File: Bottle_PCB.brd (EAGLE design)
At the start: 100 x 50 mm, 96 parts, among them IC1 LP2985-33DBV, J1 GROVE-4P-2.0-SMD, Q1 8.000 MHz, Q5 ZVN 3306 F, Q6 ZVN 3306 F, Q7 ZVN 3306 F, U1 USD-SOCKETNEW, U3 CN3065-1320040P1

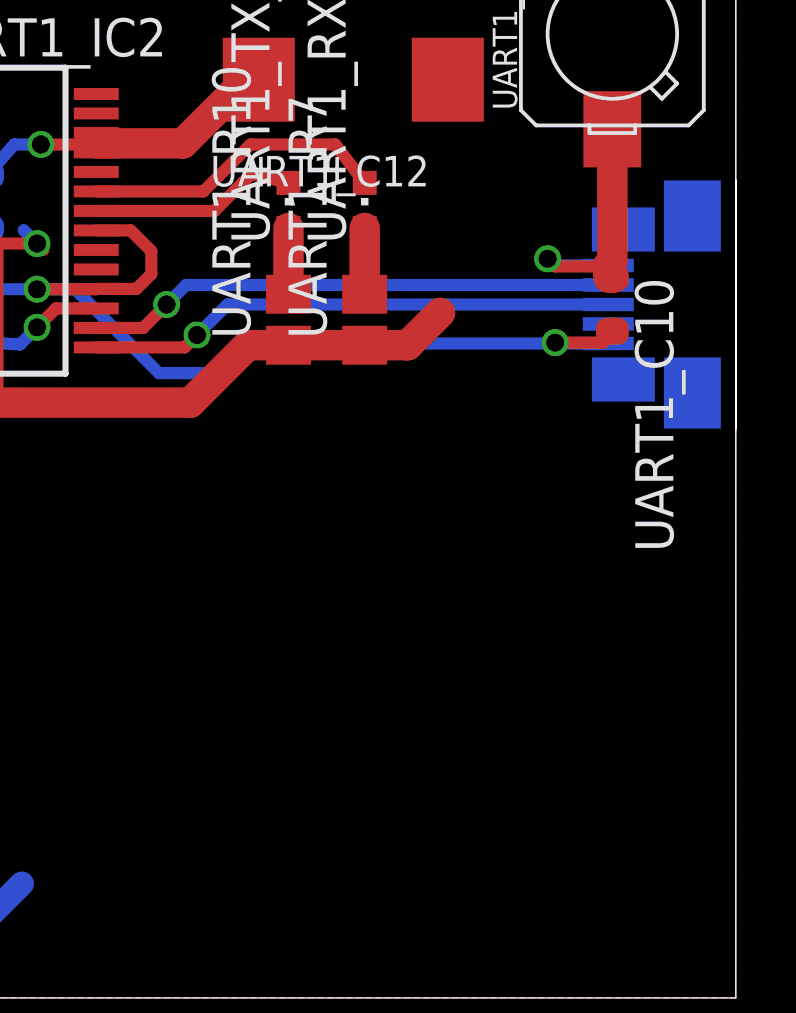
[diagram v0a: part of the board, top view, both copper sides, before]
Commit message: - replaces mini USB B connector with SparkFun version
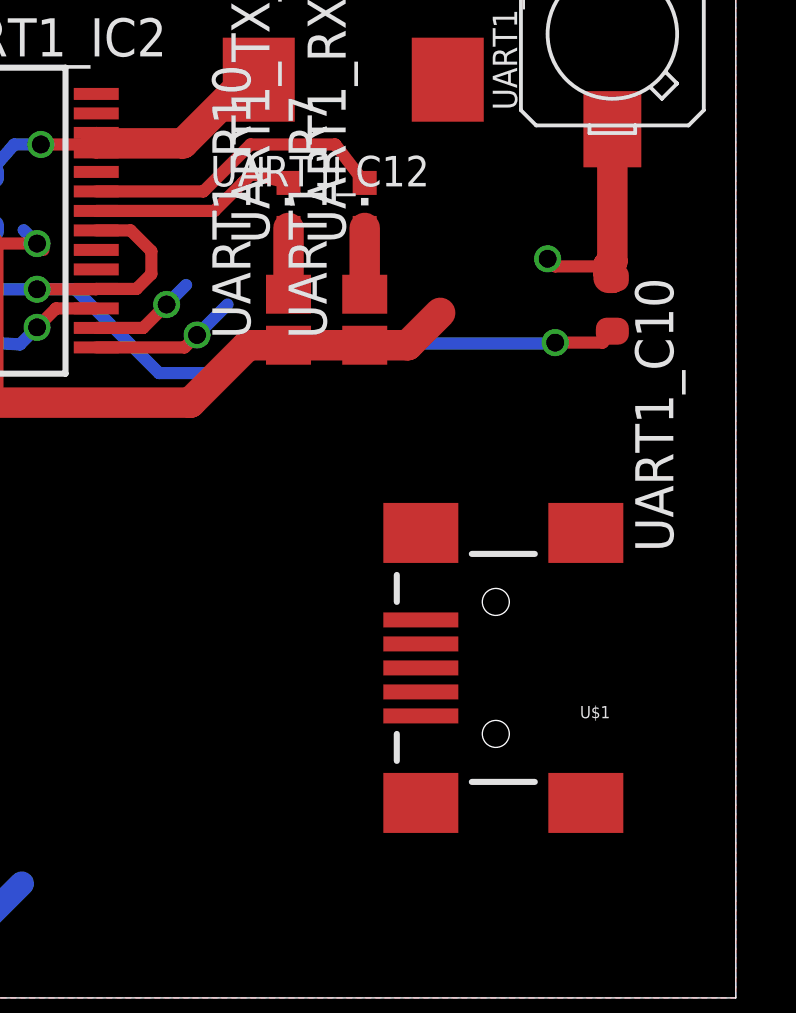
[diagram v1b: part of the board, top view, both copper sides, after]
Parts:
- removed USB1: MOLEX-47346-0001, usb_con-update:MOLEX-47364-0001
- added U$1: USB-MINIB-5PIN, SparkFun-Connectors:USB-MINIB
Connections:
- net GND: now also U$1.GND; no longer USB1.5
- net N$10: now also U$1.D+; no longer USB1.3
- net N$12: now also U$1.VBUS; no longer USB1.1
- net N$4: now also U$1.D-; no longer USB1.2
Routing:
- net N$4: track 17.7 -> 3.59 mm
- net N$10: track 17.7 -> 4.97 mm
- net N$12: track 9.74 -> 7.93 mm
- net GND: track 331.2 -> 329.5 mm
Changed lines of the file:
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@@
 <attribute name="OC_FARNELL" value="176432" x="58.1025" y="3.4925" size="1.778" layer="27" rot="R180" display="off"/>
-</element>
-<element name="USB1" library="usb_con-update" package="MOLEX-47364-0001" value="MOLEX-47346-0001" x="98.552" y="23.114" smashed="yes" rot="MR0">
-<attribute name="NAME" x="99.802" y="27.714" size="1.27" layer="22" rot="MR0"/>
 </element>
 <element name="D1" library="diode" package="SOD-123_MINI-SMA" value="CGRM4001-G" x="57.4675" y="10.4775" rot="R90"/>
@@
 <element name="C_V_LIPO_USB" library="_E" package="SMC_D" value="10µ/10V" x="-65" y="-301"/>
 <element name="UART1_C1" library="Arduino-SmartPrj" package="C0603-ROUND" value="10n" x="-68" y="-308"/>
+<element name="U$1" library="SparkFun-Connectors" package="USB-MINIB" value="USB-MINIB-5PIN" x="92" y="11" rot="R180"/>
 </elements>
 <signals>
@@
 <contactref element="RESET_SW" pad="2"/>
 <wire x1="78.682" y1="28.183" x2="78.682" y2="28.48479375" width="0.4064" layer="1"/>
-<contactref element="USB1" pad="5"/>
 <contactref element="C2" pad="1"/>
 <contactref element="C3" pad="1"/>
@@
 <wire x1="76.708" y1="23.622" x2="75.118" y2="23.622" width="0.4064" layer="16"/>
 <wire x1="75.118" y1="23.622" x2="75.057" y2="23.622" width="0.4064" layer="16"/>
-<wire x1="95.752" y1="21.814" x2="94.01" y2="21.814" width="0.4064" layer="16"/>
 <wire x1="94.01" y1="21.814" x2="93.98" y2="21.844" width="0.4064" layer="16"/>
 <via x="93.98" y="21.844" extent="1-16" drill="0.6"/>
@@
 <contactref element="C_V_LIPO_USB" pad="-"/>
 <contactref element="UART1_C1" pad="2"/>
+<contactref element="U$1" pad="GND"/>
 <wire x1="-44" y1="-175.25" x2="-47.95" y2="-183" width="0" layer="19" extent="1-1"/>
 <wire x1="-44" y1="-168.25" x2="-44" y2="-175.25" width="0" layer="19" extent="1-1"/>
@@
 <wire x1="55" y1="35" x2="51.1175" y2="41.5925" width="0" layer="19" extent="1-1"/>
 <wire x1="3" y1="16" x2="1.4405" y2="25.568" width="0" layer="19" extent="1-1"/>
+<wire x1="89.5" y1="12.6" x2="94.01" y2="21.814" width="0" layer="19" extent="1-16"/>
 </signal>
 <signal name="AREF">
@@
 <signal name="N$4">
 <contactref element="UART1_IC2" pad="16"/>
-<contactref element="USB1" pad="2"/>
-<wire x1="95.752" y1="23.764" x2="81.676" y2="23.764" width="0.4064" layer="16"/>
 <wire x1="81.676" y1="23.764" x2="81.026" y2="23.114" width="0.4064" layer="16"/>
 <via x="81.026" y="23.114" extent="1-16" drill="0.6"/>
 <wire x1="81.026" y1="23.114" x2="80.245" y2="22.333" width="0.4064" layer="1"/>
 <wire x1="80.245" y1="22.333" x2="78.682" y2="22.333" width="0.4064" layer="1"/>
+<contactref element="U$1" pad="D-"/>
+<wire x1="80.245" y1="22.333" x2="89.5" y2="10.2" width="0" layer="19" extent="1-1"/>
 </signal>
 <signal name="N$10">
 <contactref element="UART1_IC2" pad="15"/>
-<contactref element="USB1" pad="3"/>
-<wire x1="95.752" y1="23.114" x2="83.058" y2="23.114" width="0.4064" layer="16"/>
 <wire x1="83.058" y1="23.114" x2="82.042" y2="22.098" width="0.4064" layer="16"/>
 <via x="82.042" y="22.098" extent="1-16" drill="0.6"/>
 <wire x1="82.042" y1="22.098" x2="81.627" y2="21.683" width="0.4064" layer="1"/>
 <wire x1="81.627" y1="21.683" x2="78.682" y2="21.683" width="0.4064" layer="1"/>
+<contactref element="U$1" pad="D+"/>
+<wire x1="81.627" y1="21.683" x2="89.5" y2="11" width="0" layer="19" extent="1-1"/>
 </signal>
 <signal name="N$11">
@@
 <contactref element="UART1_C10" pad="1"/>
 <contactref element="UART1_L2" pad="1"/>
-<contactref element="USB1" pad="1"/>
 <wire x1="95.758" y1="24.003" x2="95.885" y2="24.003" width="1.016" layer="1"/>
 <wire x1="95.885" y1="28.956" x2="95.885" y2="24.547" width="1.016" layer="1"/>
@@
 <wire x1="95.752" y1="24.414" x2="95.752" y2="24.197" width="1.016" layer="1"/>
 <wire x1="95.752" y1="24.197" x2="95.885" y2="24.003" width="1.016" layer="1"/>
-<wire x1="95.752" y1="24.414" x2="93.95" y2="24.414" width="0.4064" layer="16"/>
 <wire x1="93.95" y1="24.414" x2="93.726" y2="24.638" width="0.4064" layer="16"/>
 <via x="93.726" y="24.638" extent="1-16" drill="0.6"/>
@@
 <wire x1="93.98" y1="24.384" x2="95.565" y2="24.384" width="0.4064" layer="1"/>
 <wire x1="95.565" y1="24.384" x2="95.885" y2="24.003" width="0.4064" layer="1"/>
+<contactref element="U$1" pad="VBUS"/>
+<wire x1="89.5" y1="9.4" x2="93.98" y2="24.384" width="0" layer="19" extent="1-1"/>
 </signal>
 <signal name="N$13">

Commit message: - cleaned up and unified many discrete components - set Reichelt Order Numbers for all capacitors
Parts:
- removed D1: CGRM4001-G, diode:SOD-123_MINI-SMA
- removed UART1_D_RESET: 1N4848, _D:MINIMELF
- added D5, D6: MSS1P2U, Seed-Discrete:D1005
- added R_WAKEUP: 10k, Arduino-SmartPrj:R0603-ROUND
- C1, C11, C12, C16, C2, C3, C4, C6, C7, C8, C9: device quantum-sensor:C0805 -> Arduino-SmartPrj:C0603-ROUND
- C10, C5: device rcl:SMC_D -> Arduino-SmartPrj:C1210
- C13: device rcl:C0805 -> Arduino-SmartPrj:C1210
- C14, C15: device resistor:C0603 -> Arduino-SmartPrj:C0603-ROUND
- R1, R10, R11, R16, R17, R18, R19, R20, R21: device rcl:R0603 -> Arduino-SmartPrj:R0603-ROUND
- R12, R13: value 4k7 -> 10k; device resistor:R0603 -> Arduino-SmartPrj:R0603-ROUND
- R14, R15, R8, R9: device resistor:R0603 -> Arduino-SmartPrj:R0603-ROUND
- R2, R3, R4, R5, R6, R7: device rcl:M1206 -> Arduino-SmartPrj:R0603-ROUND
- R_RESET, UART1_R10, UART1_R7: device quantum-sensor:R0805 -> Arduino-SmartPrj:R0603-ROUND
- UART1_R6: device _R:R0805 -> Arduino-SmartPrj:R0603-ROUND
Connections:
- new net N$16: C12.2, R_WAKEUP.1, SW_WAKEUP.3, SW_WAKEUP.4
- net +3V3: now also D6.-; no longer D1.C
- net BEE_VCC: now also C10.1; no longer C10.+
- net FTDI_DTR: now also D5.-; no longer UART1_D_RESET.C
- net GND: now also C10.2, C5.2; no longer C10.-, C5.-
- net MCU_RST: now also D5.+, D6.+; no longer D1.A, UART1_D_RESET.A
- net N$31: now also C5.1; no longer C5.+
- net PB1_INT_BUTTON: no longer C12.2, SW_WAKEUP.3, SW_WAKEUP.4
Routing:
- net GND: track 329.5 -> 294.3 mm, vias 26 -> 25
- net MCU_RST: track 72.3 -> 60.3 mm
- net +3V3: track 266.4 -> 255.2 mm, vias 10 -> 9
- net PB1_INT_BUTTON: track 10.2 -> 0.00 mm
- net N$31: track 24.6 -> 26.4 mm
- net N$33: track 33.5 -> 35.2 mm
- net PC2_SD_OFF: track 22.3 -> 22.8 mm

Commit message: - unified, replaced and checked all components - added vendor IDs and order information to all components - generated BOMs
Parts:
- removed C_3V3, C_VIN, C_V_LIPO_USB: 10µ/10V, _E:SMC_D
- removed UART1_C12: 10µ, _E:SMC_D
- added C17, C18, C19, C20: 10µF / 16V, Arduino-SmartPrj:C0805
- ATMEGA1284P-AU: value ATMEGA644A -> Reichelt ATMEGA 1284P-AU
- GROOVE_A6_A7, GROOVE_D7_D8, GROOVE_I2C: value GROVE-4P-2.0-SMD -> GROVE-4P-2.0-SMD Seed ACC39145O
- IC1: value LP2985-33DBV -> LP2985-33DBV, Farnell 2395925
- ISP1: value AVRISP-6 -> Reichelt WSL 6G
- Q1: value 8.000 MHz -> 16.000 MHz; device crystal:HC18U-V -> crystal:HC49U-V
- Q5, Q6, Q7: value ZVN 3306 F -> Reichelt ZVN 3306 F
- R17: value 330 (20mA) or 2k -> 330 (20mA) or 2k2
- R5: value 20k -> 10k
- T_LIPO_USB: value (none) -> Reichelt IRLML 6402
- U1: value USD-SOCKETNEW -> Sparkfun PRT-00127
- U2: value (none) -> Seed BLE Bee - Based on HM-11 Module sowie Bluetooth V4.0 HM-11 BLE Module
- U3: value CN3065-1320040P1 -> CN3065-1320040P1, Aliexpress Such as rhyme new original CN3065 DFN8 lithium battery charge management / protection chip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
- UART1_IC2: value FT232RL -> Reichelt FT 232 RL
- UART1_L2: device _Trafo_Spule:PIS2408 -> rcl:L1812
- UART1_R10, UART1_R7: value 1k -> 2k2
- USB_CONNECTOR: value USB-MINIB-5PIN -> USB-MINIB-5PIN Sparkfun PRT-00587
- XBEE_SOCKET: value XBEE-1B3 -> 2x Reichelt BL 1X10G SMD2,00
- renumbered ATMEGA1284 to ATMEGA1284P-AU, J1 to GROOVE_A6_A7, U$1 to USB_CONNECTOR
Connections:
- net +3V3: now also C18.1; no longer C_3V3.+
- net +5V: now also C20.1; no longer UART1_C12.+
- net GND: now also C17.2, C18.2, C19.2, C20.2; no longer C_3V3.-, C_VIN.-, C_V_LIPO_USB.-, UART1_C12.-
- net VIN: now also C19.1; no longer C_VIN.+
- net V_LIPO_USB: now also C17.1; no longer C_V_LIPO_USB.+
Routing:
- net N$12: track 7.93 -> 9.16 mm

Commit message: - merged BOMs - BOM_Merged.csv is checked for correctness and completeness - minor adjustments in Device Values for unification
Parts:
- C1: value 22p -> 22pF
- C10, C5: value 1µ -> 1µF
- C11, C12, C2, C3, C4, C6, C7, C8, UART1_C11, UART1_C2: value 100n -> 100nF
- C9: value 22p -> 22pf
- UART1_C10: value 10n -> 10nF
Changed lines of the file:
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@@
 <attribute name="VALUE" x="55.88" y="11.7475" size="1.27" layer="27" rot="R90"/>
 </element>
-<element name="C9" library="Arduino-SmartPrj" package="C0603-ROUND" value="22p" x="61.2648" y="20.8788" smashed="yes" rot="R270">
+<element name="C9" library="Arduino-SmartPrj" package="C0603-ROUND" value="22pf" x="61.2648" y="20.8788" smashed="yes" rot="R270">
 <attribute name="NAME" x="62.5348" y="22.1488" size="1.27" layer="25" rot="R270"/>
 <attribute name="VALUE" x="60.6298" y="19.6088" size="1.27" layer="27" rot="R270"/>
 </element>
-<element name="C1" library="Arduino-SmartPrj" package="C0603-ROUND" value="22p" x="61.2648" y="24.3078" smashed="yes" rot="R90">
+<element name="C1" library="Arduino-SmartPrj" package="C0603-ROUND" value="22pF" x="61.2648" y="24.3078" smashed="yes" rot="R90">
 <attribute name="NAME" x="59.9948" y="23.0378" size="1.27" layer="25" rot="R90"/>
 <attribute name="VALUE" x="62.2173" y="25.5778" size="1.27" layer="27" rot="R90"/>
 </element>
-<element name="C7" library="Arduino-SmartPrj" package="C0603-ROUND" value="100n" x="36.5125" y="21.59" smashed="yes" rot="R270">
+<element name="C7" library="Arduino-SmartPrj" package="C0603-ROUND" value="100nF" x="36.5125" y="21.59" smashed="yes" rot="R270">
 <attribute name="NAME" x="37.7825" y="22.86" size="1.27" layer="25" rot="R270"/>
 <attribute name="VALUE" x="38.735" y="20.0025" size="1.27" layer="27" rot="R90"/>
@@
 <attribute name="OC_FARNELL" value="1455123" x="46.0375" y="21.2725" size="1.778" layer="27" rot="R180" display="off"/>
 </element>
-<element name="C6" library="Arduino-SmartPrj" package="C0603-ROUND" value="100n" x="47.625" y="21.59" rot="MR180"/>
+<element name="C6" library="Arduino-SmartPrj" package="C0603-ROUND" value="100nF" x="47.625" y="21.59" rot="MR180"/>
 <element name="UART1_IC2" library="FTDI" package="SSOP28" value="Reichelt FT 232 RL" x="75.057" y="25.908" rot="R270"/>
-<element name="UART1_C2" library="Arduino-SmartPrj" package="C0603-ROUND" value="100n" x="75.057" y="22.733" rot="MR90"/>
-<element name="UART1_C10" library="Arduino-SmartPrj" package="C0603-ROUND" value="10n" x="95.885" y="23.114" rot="R270"/>
-<element name="UART1_C11" library="Arduino-SmartPrj" package="C0603-ROUND" value="100n" x="75.057" y="26.543" rot="MR90"/>
+<element name="UART1_C2" library="Arduino-SmartPrj" package="C0603-ROUND" value="100nF" x="75.057" y="22.733" rot="MR90"/>
+<element name="UART1_C10" library="Arduino-SmartPrj" package="C0603-ROUND" value="10nF" x="95.885" y="23.114" rot="R270"/>
+<element name="UART1_C11" library="Arduino-SmartPrj" package="C0603-ROUND" value="100nF" x="75.057" y="26.543" rot="MR90"/>
 <element name="UART1_R6" library="Arduino-SmartPrj" package="R0603-ROUND" value="10k" x="68.3895" y="21.7805" rot="R180"/>
 <element name="UART1_R7" library="Arduino-SmartPrj" package="R0603-ROUND" value="2k2" x="87.63" y="22.606" rot="R90"/>
@@
 <attribute name="OC_FARNELL" value="176432" x="58.1025" y="3.4925" size="1.778" layer="27" rot="R180" display="off"/>
 </element>
-<element name="C2" library="Arduino-SmartPrj" package="C0603-ROUND" value="100n" x="45.085" y="19.05" rot="MR270"/>
-<element name="C3" library="Arduino-SmartPrj" package="C0603-ROUND" value="100n" x="44.7675" y="22.86" rot="MR90"/>
+<element name="C2" library="Arduino-SmartPrj" package="C0603-ROUND" value="100nF" x="45.085" y="19.05" rot="MR270"/>
+<element name="C3" library="Arduino-SmartPrj" package="C0603-ROUND" value="100nF" x="44.7675" y="22.86" rot="MR90"/>
 <element name="ISP1" library="adafruit" package="AVRISP" value="Reichelt WSL 6G" x="51.7525" y="46.0375"/>
 <element name="I2C" library="con-lstb" package="MA04-1" value="" x="43.18" y="34.29">
@@
 <element name="R5" library="Arduino-SmartPrj" package="R0603-ROUND" value="10k" x="21.7678" y="29.2481"/>
 <element name="R6" library="Arduino-SmartPrj" package="R0603-ROUND" value="100k" x="17.9451" y="27.7495" rot="R90"/>
-<element name="C4" library="Arduino-SmartPrj" package="C0603-ROUND" value="100n" x="3.4925" y="37.7825" rot="MR90"/>
-<element name="C5" library="Arduino-SmartPrj" package="C1210" value="1µ" x="12.3825" y="45.085"/>
+<element name="C4" library="Arduino-SmartPrj" package="C0603-ROUND" value="100nF" x="3.4925" y="37.7825" rot="MR90"/>
+<element name="C5" library="Arduino-SmartPrj" package="C1210" value="1µF" x="12.3825" y="45.085"/>
 <element name="R7" library="Arduino-SmartPrj" package="R0603-ROUND" value="10k" x="29.5275" y="6.0325" rot="MR0"/>
-<element name="C8" library="Arduino-SmartPrj" package="C0603-ROUND" value="100n" x="22.225" y="5.715"/>
-<element name="C10" library="Arduino-SmartPrj" package="C1210" value="1µ" x="24.3975" y="9.4" rot="MR90"/>
+<element name="C8" library="Arduino-SmartPrj" package="C0603-ROUND" value="100nF" x="22.225" y="5.715"/>
+<element name="C10" library="Arduino-SmartPrj" package="C1210" value="1µF" x="24.3975" y="9.4" rot="MR90"/>
 <element name="Q6" library="transistor-small-signal" package="SOT23" value="Reichelt ZVN 3306 F" x="31.115" y="9.8425" rot="MR0"/>
 <element name="R8" library="Arduino-SmartPrj" package="R0603-ROUND" value="100k" x="35.433" y="8.763" rot="MR0"/>
@@
 <attribute name="OC_FARNELL" value="176432" x="45.72" y="3.4925" size="1.778" layer="27" rot="R180" display="off"/>
 </element>
-<element name="C12" library="Arduino-SmartPrj" package="C0603-ROUND" value="100n" x="39.37" y="3.4925" rot="R90"/>
+<element name="C12" library="Arduino-SmartPrj" package="C0603-ROUND" value="100nF" x="39.37" y="3.4925" rot="R90"/>
 <element name="IOL" library="con-lsta" package="FE08" value="" x="5" y="-11">
 <attribute name="OC_NEWARK" value="unknown" x="5" y="-11" size="1.778" layer="27" display="off"/>
@@
 <attribute name="OC_FARNELL" value="176432" x="-39" y="-73" size="1.778" layer="27" display="off"/>
 </element>
-<element name="C11" library="Arduino-SmartPrj" package="C0603-ROUND" value="100n" x="-31" y="-92"/>
+<element name="C11" library="Arduino-SmartPrj" package="C0603-ROUND" value="100nF" x="-31" y="-92"/>
 <element name="JP1" library="SparkFun-Connectors" package="1X06" value="" x="-31" y="-99"/>
 <element name="R9" library="Arduino-SmartPrj" package="R0603-ROUND" value="1k" x="-31" y="-103"/>

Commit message: - replaced Diodes with lower quality version, as they are easier to get - added important BOM information
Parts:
- D2, D3, D4, D5, D6: value MSS1P2U -> MSS1P2L
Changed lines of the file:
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@@
 <element name="SOLAR" library="Seed-Battery-Connector" package="JST-2.0" value="" x="-45" y="-176"/>
 <element name="C13" library="Arduino-SmartPrj" package="C1210" value="1µF" x="-47" y="-183"/>
-<element name="D2" library="Seed-Discrete" package="D1005" value="MSS1P2U" x="-46" y="-189"/>
-<element name="D3" library="Seed-Discrete" package="D1005" value="MSS1P2U" x="-46" y="-192"/>
-<element name="D4" library="Seed-Discrete" package="D1005" value="MSS1P2U" x="-46" y="-195"/>
+<element name="D2" library="Seed-Discrete" package="D1005" value="MSS1P2L" x="-46" y="-189"/>
+<element name="D3" library="Seed-Discrete" package="D1005" value="MSS1P2L" x="-46" y="-192"/>
+<element name="D4" library="Seed-Discrete" package="D1005" value="MSS1P2L" x="-46" y="-195"/>
 <element name="SJ2" library="jumper" package="SJ_2" value="" x="-46" y="-201"/>
 <element name="SJ4" library="jumper" package="SJ_2" value="" x="-46" y="-206"/>
@@
 <element name="USB_CONNECTOR" library="SparkFun-Connectors" package="USB-MINIB" value="USB-MINIB-5PIN Sparkfun PRT-00587" x="92" y="11" rot="R180"/>
 <element name="R_WAKEUP" library="Arduino-SmartPrj" package="R0603-ROUND" value="10k" x="-68" y="-314"/>
-<element name="D5" library="Seed-Discrete" package="D1005" value="MSS1P2U" x="-67" y="-319"/>
-<element name="D6" library="Seed-Discrete" package="D1005" value="MSS1P2U" x="-67" y="-324"/>
+<element name="D5" library="Seed-Discrete" package="D1005" value="MSS1P2L" x="-67" y="-319"/>
+<element name="D6" library="Seed-Discrete" package="D1005" value="MSS1P2L" x="-67" y="-324"/>
 <element name="C17" library="Arduino-SmartPrj" package="C0805" value="10µF / 16V" x="-68" y="-330"/>
 <element name="C18" library="Arduino-SmartPrj" package="C0805" value="10µF / 16V" x="-68" y="-334"/>
